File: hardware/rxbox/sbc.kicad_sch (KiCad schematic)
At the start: 0 parts

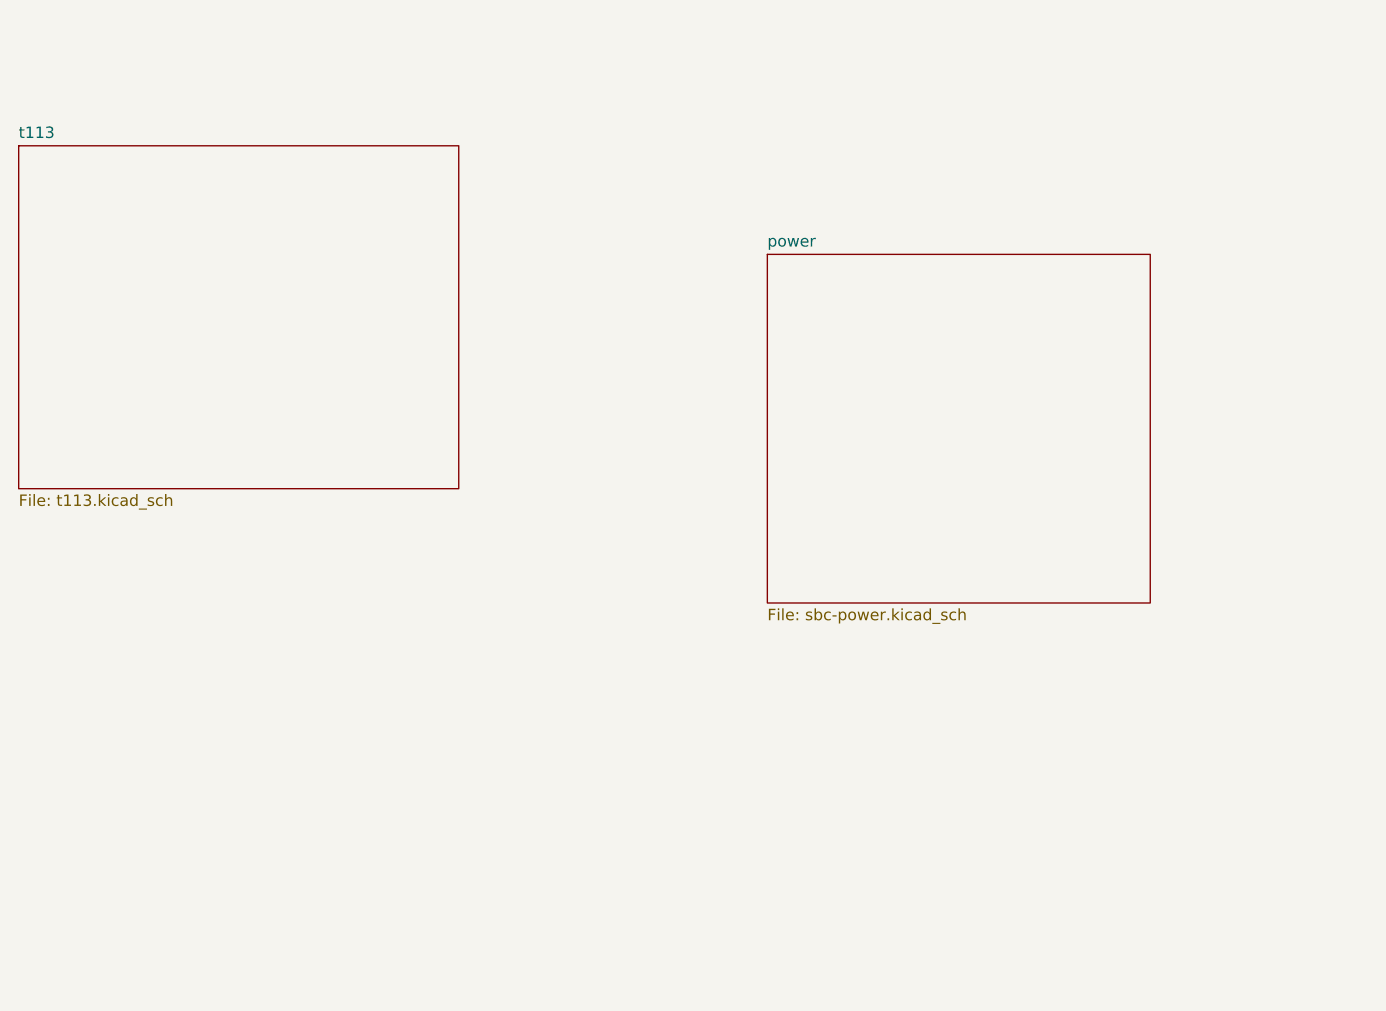
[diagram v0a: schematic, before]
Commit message: connect power + t113 sheets
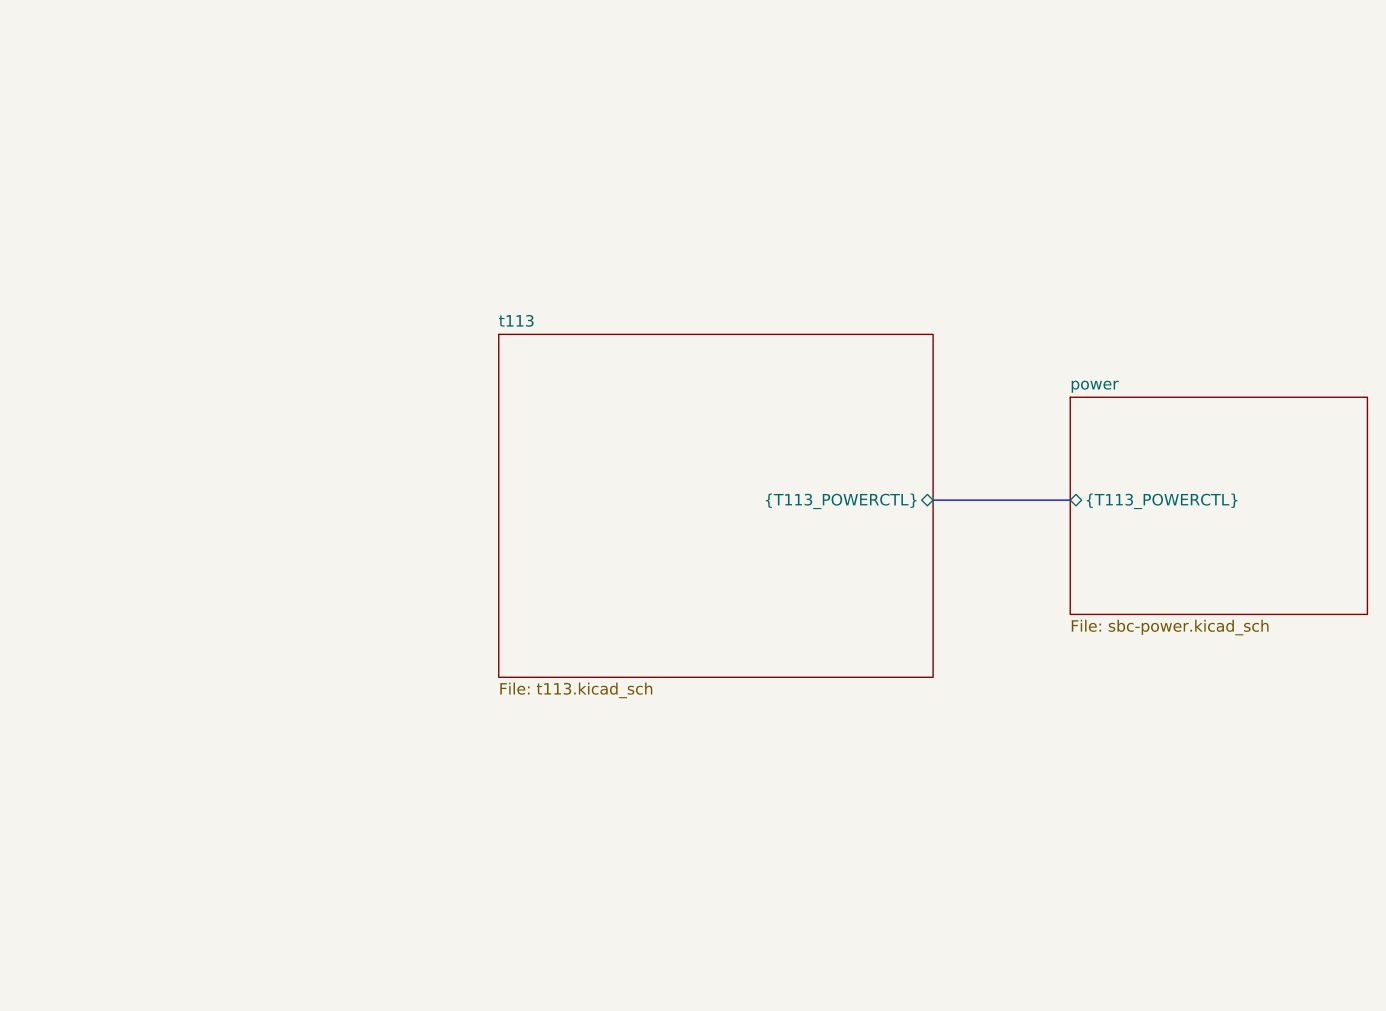
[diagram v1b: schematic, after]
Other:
- sheet power ports: added {T113_POWERCTL}; removed none
- sheet t113 ports: added {T113_POWERCTL}; removed none
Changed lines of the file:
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@@
 	(generator_version "10.0")
 	(paper "A4")
+	(bus
+		(pts
+			(xy 146.05 81.28) (xy 161.29 81.28)
+		)
+		(stroke
+			(width 0)
+			(type default)
+		)
+	)
 	(sheet
-		(at 44.45 41.91)
-		(size 48.895 38.1)
+		(at 97.79 62.865)
+		(size 48.26 38.1)
 		(exclude_from_sim no)
 		(in_bom yes)
@@
 		)
 		(property "Sheetname" "t113"
-			(at 44.45 41.1984 0)
+			(at 97.79 62.1534 0)
 			(show_name no)
 			(do_not_autoplace no)
@@
 		)
 		(property "Sheetfile" "t113.kicad_sch"
-			(at 44.45 80.5946 0)
+			(at 97.79 101.5496 0)
 			(show_name no)
 			(do_not_autoplace no)
@@
 				)
 				(justify left top)
+			)
+		)
+		(pin "{T113_POWERCTL}" bidirectional
+			(at 146.05 81.28 0)
+			(effects
+				(font
+					(size 1.27 1.27)
+				)
+				(justify right)
 			)
 		)
@@
 	)
 	(sheet
-		(at 127.635 53.975)
-		(size 42.545 38.735)
+		(at 161.29 69.85)
+		(size 33.02 24.13)
 		(exclude_from_sim no)
 		(in_bom yes)
@@
 		)
 		(property "Sheetname" "power"
-			(at 127.635 53.2634 0)
+			(at 161.29 69.1384 0)
 			(show_name no)
 			(do_not_autoplace no)
@@
 		)
 		(property "Sheetfile" "sbc-power.kicad_sch"
-			(at 127.635 93.2946 0)
+			(at 161.29 94.5646 0)
 			(show_name no)
 			(do_not_autoplace no)
@@
 			)
 		)
+		(pin "{T113_POWERCTL}" bidirectional
+			(at 161.29 81.28 180)
+			(effects
+				(font
+					(size 1.27 1.27)
+				)
+				(justify left)
+			)
+		)

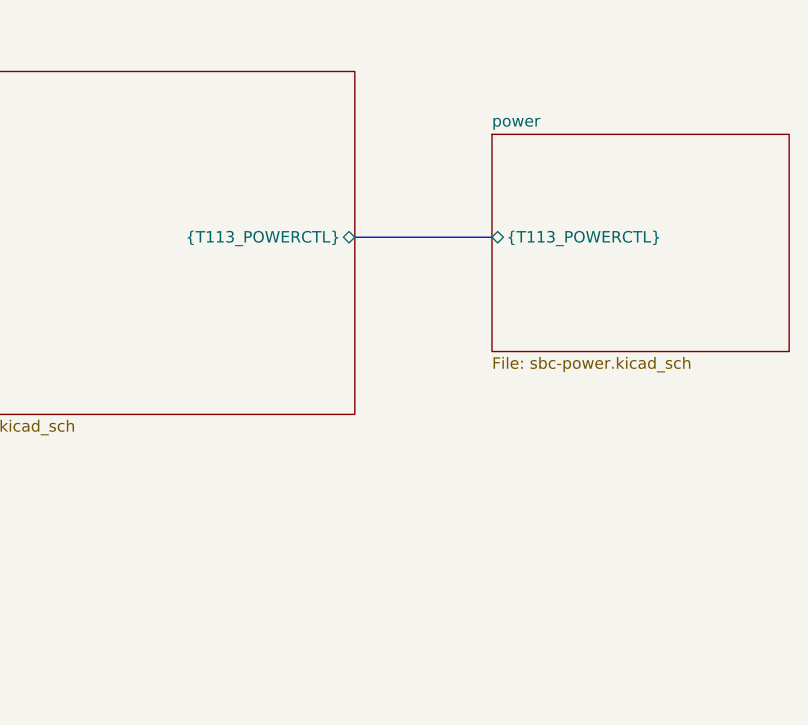
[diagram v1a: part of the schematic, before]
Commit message: finish up power, start wifi
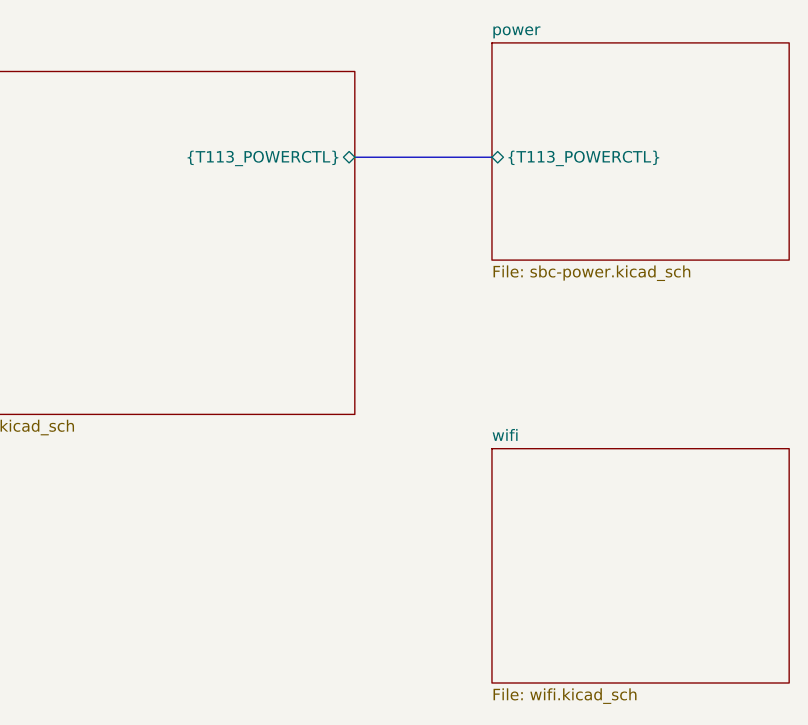
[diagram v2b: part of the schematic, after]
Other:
- added sheet wifi (wifi.kicad_sch)
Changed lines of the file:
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@@
 	(bus
 		(pts
-			(xy 146.05 81.28) (xy 161.29 81.28)
+			(xy 146.05 72.39) (xy 161.29 72.39)
 		)
 		(stroke
 			(width 0)
 			(type default)
+		)
+	)
+	(sheet
+		(at 161.29 104.775)
+		(size 33.02 26.035)
+		(exclude_from_sim no)
+		(in_bom yes)
+		(on_board yes)
+		(dnp no)
+		(fields_autoplaced yes)
+		(stroke
+			(width 0.1524)
+			(type solid)
+		)
+		(fill
+			(color 0 0 0 0)
+		)
+		(property "Sheetname" "wifi"
+			(at 161.29 104.0634 0)
+			(show_name no)
+			(do_not_autoplace no)
+			(effects
+				(font
+					(size 1.27 1.27)
+				)
+				(justify left bottom)
+			)
+		)
+		(property "Sheetfile" "wifi.kicad_sch"
+			(at 161.29 131.3946 0)
+			(show_name no)
+			(do_not_autoplace no)
+			(effects
+				(font
+					(size 1.27 1.27)
+				)
+				(justify left top)
+			)
+		)
+		(instances
+			(project "rxbox"
+				(path "/4bda69c0-d40e-4af8-940b-109cd2045912/e6dabd82-beec-4023-a66f-b67e0b07de29"
+					(page "7")
+				)
+			)
 		)
 	)
@@
 		)
 		(pin "{T113_POWERCTL}" bidirectional
-			(at 146.05 81.28 0)
+			(at 146.05 72.39 0)
 			(effects
 				(font
@@
 	)
 	(sheet
-		(at 161.29 69.85)
+		(at 161.29 59.69)
 		(size 33.02 24.13)
 		(exclude_from_sim no)
@@
 		)
 		(property "Sheetname" "power"
-			(at 161.29 69.1384 0)
+			(at 161.29 58.9784 0)
 			(show_name no)
 			(do_not_autoplace no)
@@
 		)
 		(property "Sheetfile" "sbc-power.kicad_sch"
-			(at 161.29 94.5646 0)
+			(at 161.29 84.4046 0)
 			(show_name no)
 			(do_not_autoplace no)
@@
 		)
 		(pin "{T113_POWERCTL}" bidirectional
-			(at 161.29 81.28 180)
+			(at 161.29 72.39 180)
 			(effects
 				(font

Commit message: sdio bus + new wifi module
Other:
- sheet wifi ports: added WIFI{SDIO}; removed none
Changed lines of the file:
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@@
+			)
+		)
+		(pin "WIFI{SDIO}" input
+			(at 161.29 116.84 180)
+			(effects
+				(font
+					(size 1.27 1.27)
+				)
+				(justify left)
 			)
 		)

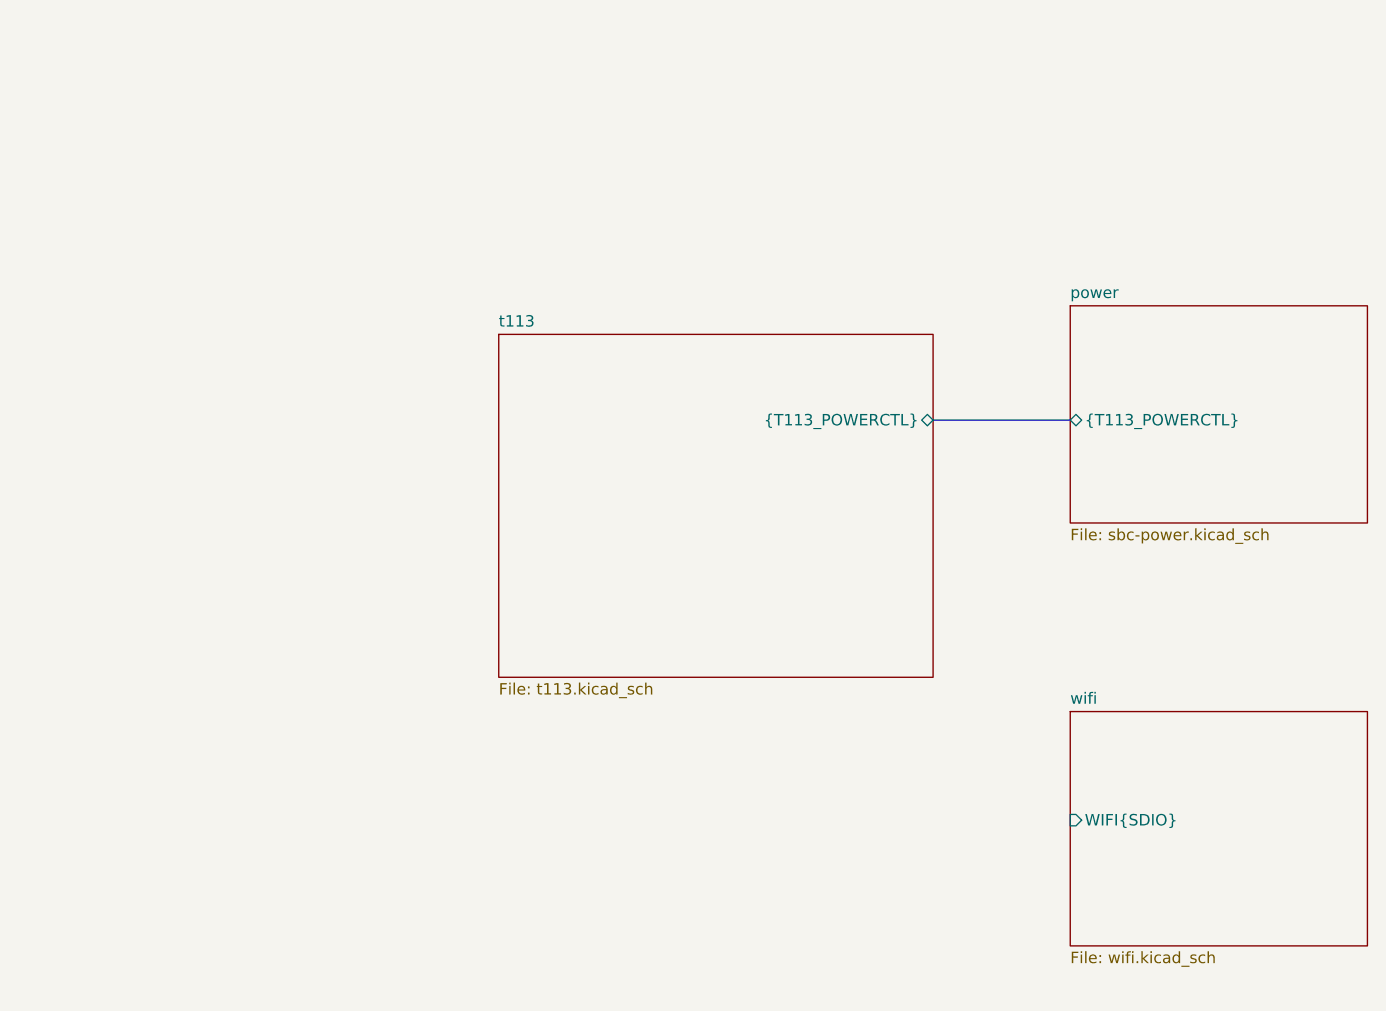
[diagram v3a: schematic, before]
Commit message: wifi updates
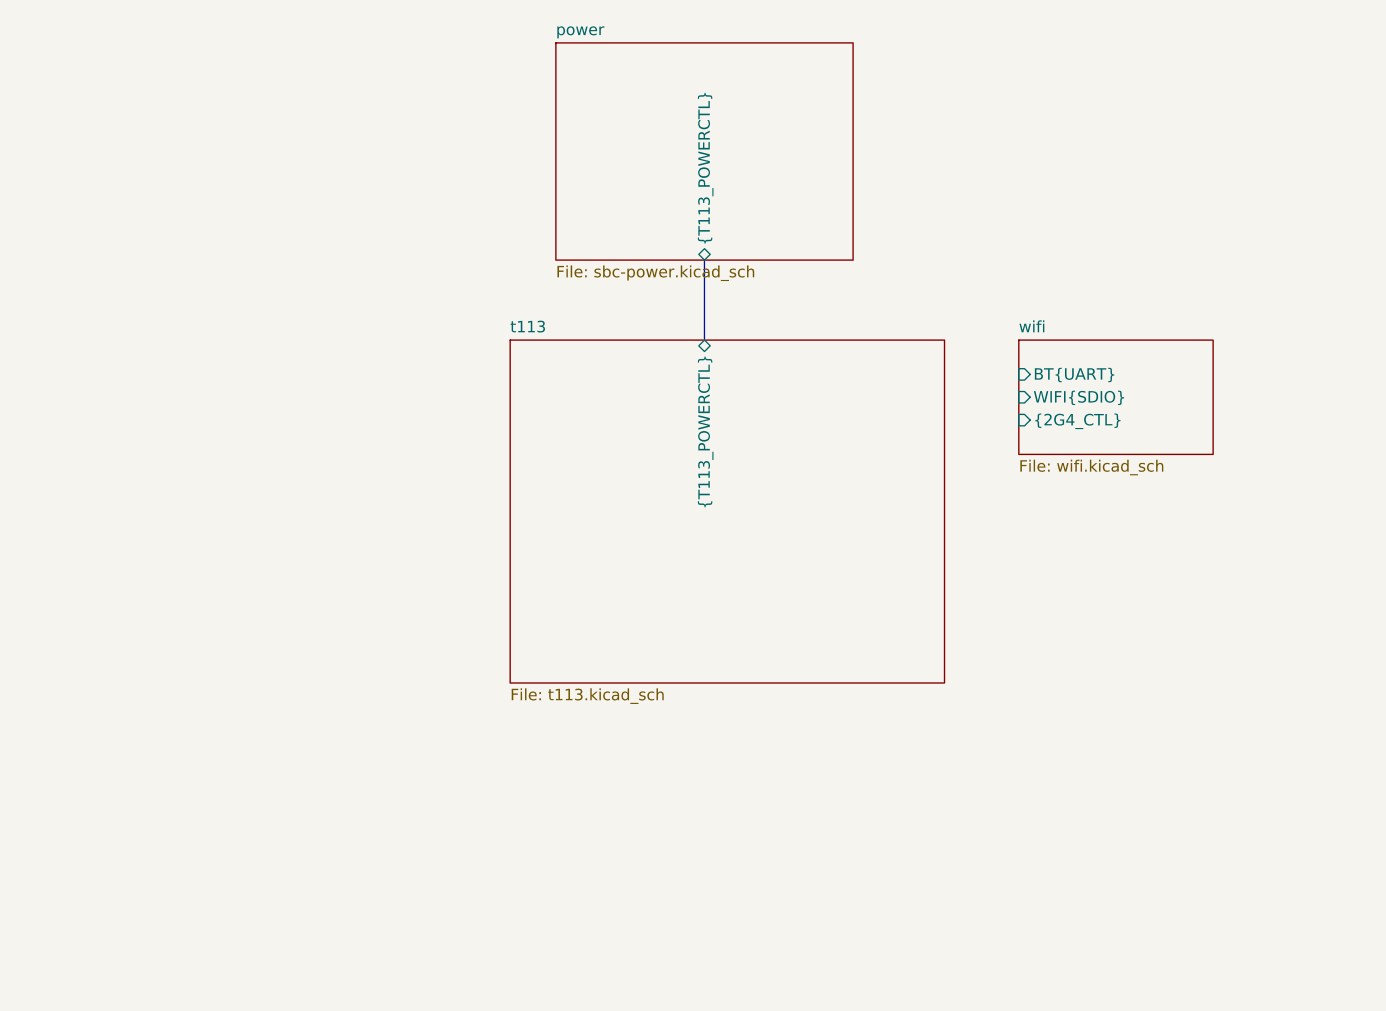
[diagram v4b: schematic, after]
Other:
- sheet wifi ports: added BT{UART}, {2G4_CTL}; removed none
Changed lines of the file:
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@@
 	(bus
 		(pts
-			(xy 146.05 72.39) (xy 161.29 72.39)
+			(xy 120.65 54.61) (xy 120.65 63.5)
 		)
 		(stroke
@@
 	)
 	(sheet
-		(at 161.29 104.775)
-		(size 33.02 26.035)
+		(at 155.575 63.5)
+		(size 21.59 12.7)
 		(exclude_from_sim no)
 		(in_bom yes)
@@
 		)
 		(property "Sheetname" "wifi"
-			(at 161.29 104.0634 0)
+			(at 155.575 62.7884 0)
 			(show_name no)
 			(do_not_autoplace no)
@@
 		)
 		(property "Sheetfile" "wifi.kicad_sch"
-			(at 161.29 131.3946 0)
+			(at 155.575 76.7846 0)
 			(show_name no)
 			(do_not_autoplace no)
@@
 		)
 		(pin "WIFI{SDIO}" input
-			(at 161.29 116.84 180)
+			(at 155.575 69.85 180)
+			(effects
+				(font
+					(size 1.27 1.27)
+				)
+				(justify left)
+			)
+		)
+		(pin "BT{UART}" input
+			(at 155.575 67.31 180)
+			(effects
+				(font
+					(size 1.27 1.27)
+				)
+				(justify left)
+			)
+		)
+		(pin "{2G4_CTL}" input
+			(at 155.575 72.39 180)
 			(effects
 				(font
@@
 	)
 	(sheet
-		(at 97.79 62.865)
+		(at 99.06 63.5)
 		(size 48.26 38.1)
 		(exclude_from_sim no)
@@
 		)
 		(property "Sheetname" "t113"
-			(at 97.79 62.1534 0)
+			(at 99.06 62.7884 0)
 			(show_name no)
 			(do_not_autoplace no)
@@
 		)
 		(property "Sheetfile" "t113.kicad_sch"
-			(at 97.79 101.5496 0)
+			(at 99.06 102.1846 0)
 			(show_name no)
 			(do_not_autoplace no)
@@
 		)
 		(pin "{T113_POWERCTL}" bidirectional
-			(at 146.05 72.39 0)
+			(at 120.65 63.5 90)
 			(effects
 				(font
@@
 	)
 	(sheet
-		(at 161.29 59.69)
+		(at 104.14 30.48)
 		(size 33.02 24.13)
 		(exclude_from_sim no)
@@
 		)
 		(property "Sheetname" "power"
-			(at 161.29 58.9784 0)
+			(at 104.14 29.7684 0)
 			(show_name no)
 			(do_not_autoplace no)
@@
 		)
 		(property "Sheetfile" "sbc-power.kicad_sch"
-			(at 161.29 84.4046 0)
+			(at 104.14 55.1946 0)
 			(show_name no)
 			(do_not_autoplace no)
@@
 		)
 		(pin "{T113_POWERCTL}" bidirectional
-			(at 161.29 72.39 180)
+			(at 120.65 54.61 270)
 			(effects
 				(font

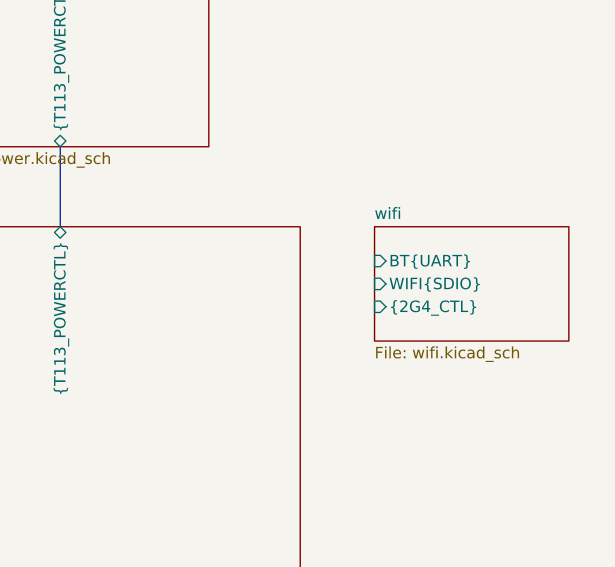
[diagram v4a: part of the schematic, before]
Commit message: wiring wifi + bt to t113
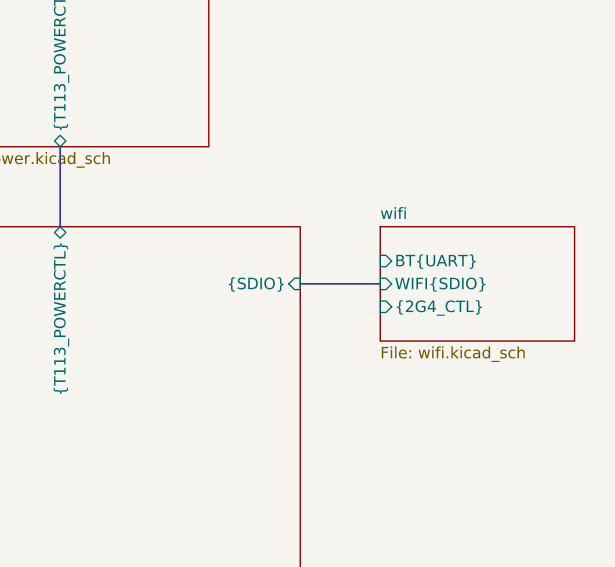
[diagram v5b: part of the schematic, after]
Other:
- sheet t113 ports: added {SDIO}; removed none
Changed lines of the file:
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@@
+	(bus
+		(pts
+			(xy 147.32 69.85) (xy 156.21 69.85)
+		)
+		(stroke
+			(width 0)
+			(type default)
+		)
+	)
 	(bus
 		(pts
@@
 	)
 	(sheet
-		(at 155.575 63.5)
+		(at 156.21 63.5)
 		(size 21.59 12.7)
 		(exclude_from_sim no)
@@
 		)
 		(property "Sheetname" "wifi"
-			(at 155.575 62.7884 0)
+			(at 156.21 62.7884 0)
 			(show_name no)
 			(do_not_autoplace no)
@@
 		)
 		(property "Sheetfile" "wifi.kicad_sch"
-			(at 155.575 76.7846 0)
+			(at 156.21 76.7846 0)
 			(show_name no)
 			(do_not_autoplace no)
@@
 		)
 		(pin "WIFI{SDIO}" input
-			(at 155.575 69.85 180)
+			(at 156.21 69.85 180)
 			(effects
 				(font
@@
 		)
 		(pin "BT{UART}" input
-			(at 155.575 67.31 180)
+			(at 156.21 67.31 180)
 			(effects
 				(font
@@
 		)
 		(pin "{2G4_CTL}" input
-			(at 155.575 72.39 180)
+			(at 156.21 72.39 180)
 			(effects
 				(font
@@
 			(effects
 				(font
+					(size 1.27 1.27)
+				)
+				(justify right)
+			)
+		)
+		(pin "{SDIO}" input
+			(at 147.32 69.85 0)
+			(effects
+				(font
